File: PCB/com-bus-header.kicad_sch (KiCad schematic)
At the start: 6 parts, among them IC8 SN75C3232EPWR

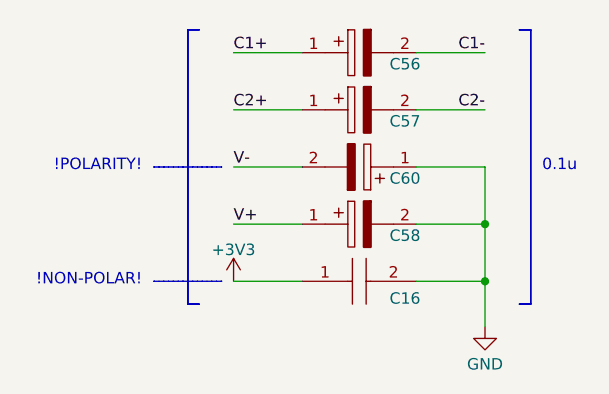
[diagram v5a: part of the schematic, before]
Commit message: silkscreen, via, and comment polishing
This isn't the change for the following issues, which were all addressed
over the last few commits, collectively. Sorry for the messiness.

Closes #30
Closes #26
Closes #25
Closes #9
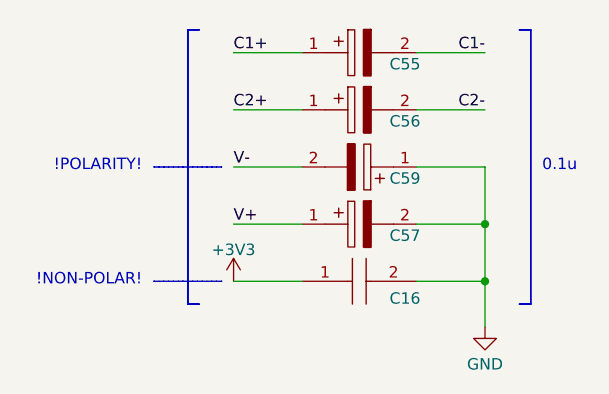
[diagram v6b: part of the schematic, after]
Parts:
- renumbered C56 to C55, C57 to C56, C58 to C57, C60 to C59
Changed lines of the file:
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@@
   (symbol (lib_id "SamacSys_Parts:UUP1H0R1MCL1GS") (at 205.105 95.885 180) (unit 1)
     (in_bom yes) (on_board yes) (dnp no)
-    (property "Reference" "C60" (at 203.835 97.155 0)
+    (property "Reference" "C59" (at 203.835 97.155 0)
       (effects (font (size 1.27 1.27)))
     )
@@
       (project "OroLink"
         (path "/e89dcd22-1250-4a5b-b778-1c95a0dd623d/a5104146-06a0-496e-bda0-1e4731a261c3"
-          (reference "C60") (unit 1)
+          (reference "C59") (unit 1)
         )
       )
@@
   (symbol (lib_id "power:GND") (at 149.225 89.535 0) (unit 1)
     (in_bom yes) (on_board yes) (dnp no) (fields_autoplaced)
-    (property "Reference" "#PWR080" (at 149.225 95.885 0)
+    (property "Reference" "#PWR078" (at 149.225 95.885 0)
       (effects (font (size 1.27 1.27)) hide)
     )
@@
       (project "OroLink"
         (path "/e89dcd22-1250-4a5b-b778-1c95a0dd623d/a5104146-06a0-496e-bda0-1e4731a261c3"
-          (reference "#PWR080") (unit 1)
+          (reference "#PWR078") (unit 1)
         )
       )
@@
   (symbol (lib_id "power:GND") (at 212.725 113.665 0) (unit 1)
     (in_bom yes) (on_board yes) (dnp no) (fields_autoplaced)
-    (property "Reference" "#PWR082" (at 212.725 120.015 0)
+    (property "Reference" "#PWR080" (at 212.725 120.015 0)
       (effects (font (size 1.27 1.27)) hide)
     )
@@
       (project "OroLink"
         (path "/e89dcd22-1250-4a5b-b778-1c95a0dd623d/a5104146-06a0-496e-bda0-1e4731a261c3"
-          (reference "#PWR082") (unit 1)
+          (reference "#PWR080") (unit 1)
         )
       )
@@
   (symbol (lib_id "SamacSys_Parts:UUP1H0R1MCL1GS") (at 192.405 102.235 0) (unit 1)
     (in_bom yes) (on_board yes) (dnp no)
-    (property "Reference" "C58" (at 203.835 103.505 0)
+    (property "Reference" "C57" (at 203.835 103.505 0)
       (effects (font (size 1.27 1.27)))
     )
@@
       (project "OroLink"
         (path "/e89dcd22-1250-4a5b-b778-1c95a0dd623d/a5104146-06a0-496e-bda0-1e4731a261c3"
-          (reference "C58") (unit 1)
+          (reference "C57") (unit 1)
         )
       )
@@
   (symbol (lib_id "power:+3V3") (at 119.38 86.995 0) (unit 1)
     (in_bom yes) (on_board yes) (dnp no) (fields_autoplaced)
-    (property "Reference" "#PWR079" (at 119.38 90.805 0)
+    (property "Reference" "#PWR077" (at 119.38 90.805 0)
       (effects (font (size 1.27 1.27)) hide)
     )
@@
       (project "OroLink"
         (path "/e89dcd22-1250-4a5b-b778-1c95a0dd623d/a5104146-06a0-496e-bda0-1e4731a261c3"
-          (reference "#PWR079") (unit 1)
+          (reference "#PWR077") (unit 1)
         )
       )
@@
         )
         (path "/e89dcd22-1250-4a5b-b778-1c95a0dd623d/a5104146-06a0-496e-bda0-1e4731a261c3"
-          (reference "C59") (unit 1)
+          (reference "C58") (unit 1)
         )
       )
@@
   (symbol (lib_id "power:+3V3") (at 184.785 108.585 0) (unit 1)
     (in_bom yes) (on_board yes) (dnp no) (fields_autoplaced)
-    (property "Reference" "#PWR081" (at 184.785 112.395 0)
+    (property "Reference" "#PWR079" (at 184.785 112.395 0)
       (effects (font (size 1.27 1.27)) hide)
     )
@@
       (project "OroLink"
         (path "/e89dcd22-1250-4a5b-b778-1c95a0dd623d/a5104146-06a0-496e-bda0-1e4731a261c3"
-          (reference "#PWR081") (unit 1)
+          (reference "#PWR079") (unit 1)
         )
       )
@@
   (symbol (lib_id "SamacSys_Parts:UUP1H0R1MCL1GS") (at 192.405 83.185 0) (unit 1)
     (in_bom yes) (on_board yes) (dnp no)
-    (property "Reference" "C56" (at 203.835 84.455 0)
+    (property "Reference" "C55" (at 203.835 84.455 0)
       (effects (font (size 1.27 1.27)))
     )
@@
       (project "OroLink"
         (path "/e89dcd22-1250-4a5b-b778-1c95a0dd623d/a5104146-06a0-496e-bda0-1e4731a261c3"
+          (reference "C55") (unit 1)
+        )
+      )
+    )
+  )
+  (symbol (lib_id "SamacSys_Parts:UUP1H0R1MCL1GS") (at 192.405 89.535 0) (unit 1)
+    (in_bom yes) (on_board yes) (dnp no)
+    (property "Reference" "C56" (at 203.835 90.805 0)
+      (effects (font (size 1.27 1.27)))
+    )
+    (property "Value" "0.1u" (at 202.565 90.805 0)
+      (effects (font (size 1.27 1.27)) hide)
+    )
+    (property "Footprint" "CAPAE430X610N" (at 201.295 88.265 0)
+      (effects (font (size 1.27 1.27)) (justify left) hide)
+    )
+    (property "Datasheet" "http://www.mouser.com/datasheet/2/293/e-uup-1513248.pdf" (at 201.295 90.805 0)
+      (effects (font (size 1.27 1.27)) (justify left) hide)
+    )
+    (property "Description" "Aluminum Electrolytic Capacitors - SMD 35volts 0.1uF 85c 4X5.8" (at 201.295 93.345 0)
+      (effects (font (size 1.27 1.27)) (justify left) hide)
+    )
+    (property "Height" "6.1" (at 201.295 95.885 0)
+      (effects (font (size 1.27 1.27)) (justify left) hide)
+    )
+    (property "Manufacturer_Name" "Nichicon" (at 201.295 98.425 0)
+      (effects (font (size 1.27 1.27)) (justify left) hide)
+    )
+    (property "Manufacturer_Part_Number" "UUP1H0R1MCL1GS" (at 201.295 100.965 0)
+      (effects (font (size 1.27 1.27)) (justify left) hide)
+    )
+    (property "Mouser Part Number" "647-UUP1H0R1MCL1GS" (at 201.295 103.505 0)
+      (effects (font (size 1.27 1.27)) (justify left) hide)
+    )
+    (property "Mouser Price/Stock" "https://www.mouser.co.uk/ProductDetail/Nichicon/UUP1H0R1MCL1GS?qs=huzeVNXgovXvQmoxbanaNw%3D%3D" (at 201.295 106.045 0)
+      (effects (font (size 1.27 1.27)) (justify left) hide)
+    )
+    (property "Arrow Part Number" "UUP1H0R1MCL1GS" (at 201.295 108.585 0)
+      (effects (font (size 1.27 1.27)) (justify left) hide)
+    )
+    (property "Arrow Price/Stock" "https://www.arrow.com/en/products/uup1h0r1mcl1gs/nichicon?region=nac" (at 201.295 111.125 0)
+      (effects (font (size 1.27 1.27)) (justify left) hide)
+    )
+    (pin "1")
+    (pin "2")
+    (instances
+      (project "OroLink"
+        (path "/e89dcd22-1250-4a5b-b778-1c95a0dd623d/a5104146-06a0-496e-bda0-1e4731a261c3"
           (reference "C56") (unit 1)
         )
       )
-    )
-  )
-  (symbol (lib_id "SamacSys_Parts:UUP1H0R1MCL1GS") (at 192.405 89.535 0) (unit 1)
-    (in_bom yes) (on_board yes) (dnp no)
-    (property "Reference" "C57" (at 203.835 90.805 0)
-      (effects (font (size 1.27 1.27)))
-    )
-    (property "Value" "0.1u" (at 202.565 90.805 0)
-      (effects (font (size 1.27 1.27)) hide)
-    )
-    (property "Footprint" "CAPAE430X610N" (at 201.295 88.265 0)
-      (effects (font (size 1.27 1.27)) (justify left) hide)
-    )
-    (property "Datasheet" "http://www.mouser.com/datasheet/2/293/e-uup-1513248.pdf" (at 201.295 90.805 0)
-      (effects (font (size 1.27 1.27)) (justify left) hide)
-    )
-    (property "Description" "Aluminum Electrolytic Capacitors - SMD 35volts 0.1uF 85c 4X5.8" (at 201.295 93.345 0)
-      (effects (font (size 1.27 1.27)) (justify left) hide)
-    )
-    (property "Height" "6.1" (at 201.295 95.885 0)
-      (effects (font (size 1.27 1.27)) (justify left) hide)
-    )
-    (property "Manufacturer_Name" "Nichicon" (at 201.295 98.425 0)
-      (effects (font (size 1.27 1.27)) (justify left) hide)
-    )
-    (property "Manufacturer_Part_Number" "UUP1H0R1MCL1GS" (at 201.295 100.965 0)
-      (effects (font (size 1.27 1.27)) (justify left) hide)
-    )
-    (property "Mouser Part Number" "647-UUP1H0R1MCL1GS" (at 201.295 103.505 0)
-      (effects (font (size 1.27 1.27)) (justify left) hide)
-    )
-    (property "Mouser Price/Stock" "https://www.mouser.co.uk/ProductDetail/Nichicon/UUP1H0R1MCL1GS?qs=huzeVNXgovXvQmoxbanaNw%3D%3D" (at 201.295 106.045 0)
-      (effects (font (size 1.27 1.27)) (justify left) hide)
-    )
-    (property "Arrow Part Number" "UUP1H0R1MCL1GS" (at 201.295 108.585 0)
-      (effects (font (size 1.27 1.27)) (justify left) hide)
-    )
-    (property "Arrow Price/Stock" "https://www.arrow.com/en/products/uup1h0r1mcl1gs/nichicon?region=nac" (at 201.295 111.125 0)
-      (effects (font (size 1.27 1.27)) (justify left) hide)
-    )
-    (pin "1")
-    (pin "2")
-    (instances
-      (project "OroLink"
-        (path "/e89dcd22-1250-4a5b-b778-1c95a0dd623d/a5104146-06a0-496e-bda0-1e4731a261c3"
-          (reference "C57") (unit 1)
-        )
-      )

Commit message: fix mouser ID on MSAST1L3YB5104KFNA01 caps
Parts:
- C16: symbol SamacSys_Parts:MSAST1L3YB5104KFNA01 -> Oro:MSAST1L3YB5104KFNA01; Mouser Part Number (none) -> 963-MSAST1L3YB5104KF; Mouser Price/Stock (none) -> https://www.mouser.de/ProductDetail/TAIYO-YUDEN/MSAST1L3YB5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
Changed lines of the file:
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@@
     )
   )
-  (symbol (lib_id "SamacSys_Parts:MSAST1L3YB5104KFNA01") (at 192.405 108.585 0) (mirror x) (unit 1)
+  (symbol (lib_id "Oro:MSAST1L3YB5104KFNA01") (at 192.405 108.585 0) (mirror x) (unit 1)
     (in_bom yes) (on_board yes) (dnp no)
     (property "Reference" "C16" (at 203.835 110.49 0)
@@
       (effects (font (size 1.27 1.27)) (justify left) hide)
     )
-    (property "Mouser Part Number" "" (at 201.295 94.615 0)
+    (property "Mouser Part Number" "963-MSAST1L3YB5104KF" (at 201.295 94.615 0)
       (effects (font (size 1.27 1.27)) (justify left) hide)
     )
-    (property "Mouser Price/Stock" "" (at 201.295 92.075 0)
+    (property "Mouser Price/Stock" "https://www.mouser.de/ProductDetail/TAIYO-YUDEN/MSAST1L3YB5104KFNA01?qs=tlsG%2FOw5FFhBwK%252BMwEZpCA%3D%3D" (at 201.295 92.075 0)
       (effects (font (size 1.27 1.27)) (justify left) hide)
     )
